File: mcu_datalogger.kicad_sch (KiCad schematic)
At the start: 25 parts, among them U1 DS1337S_, U3 24LC1025, U4 24LC1025, U5 ATMEGA328P-AU, Y1 32.768 KHz, Y2 16MHz

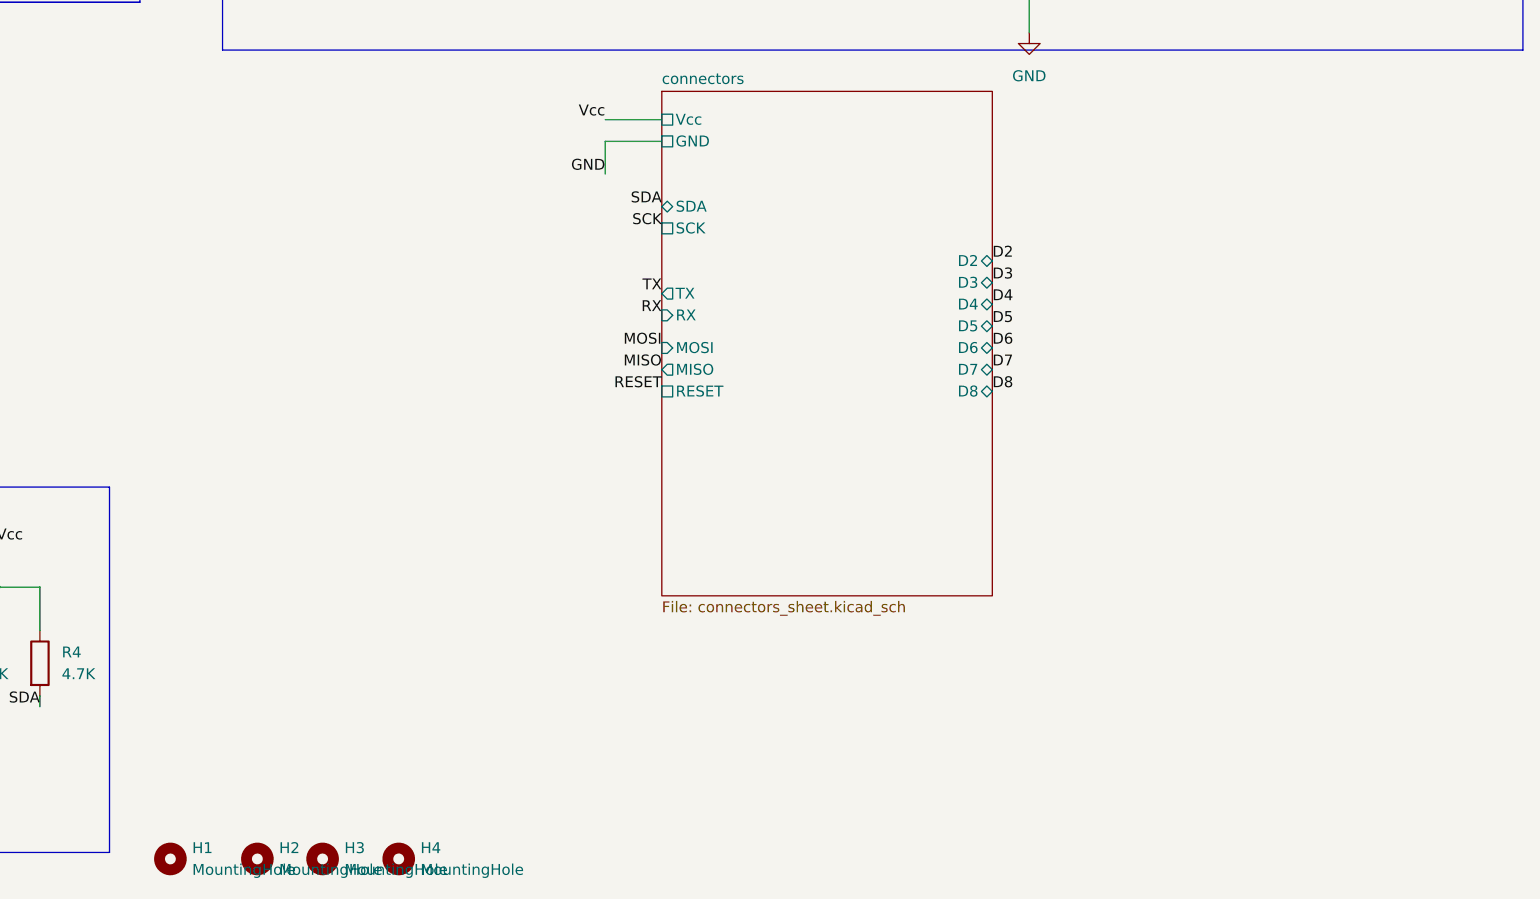
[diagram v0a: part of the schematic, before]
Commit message: Added all the Markings for Mounting Hole
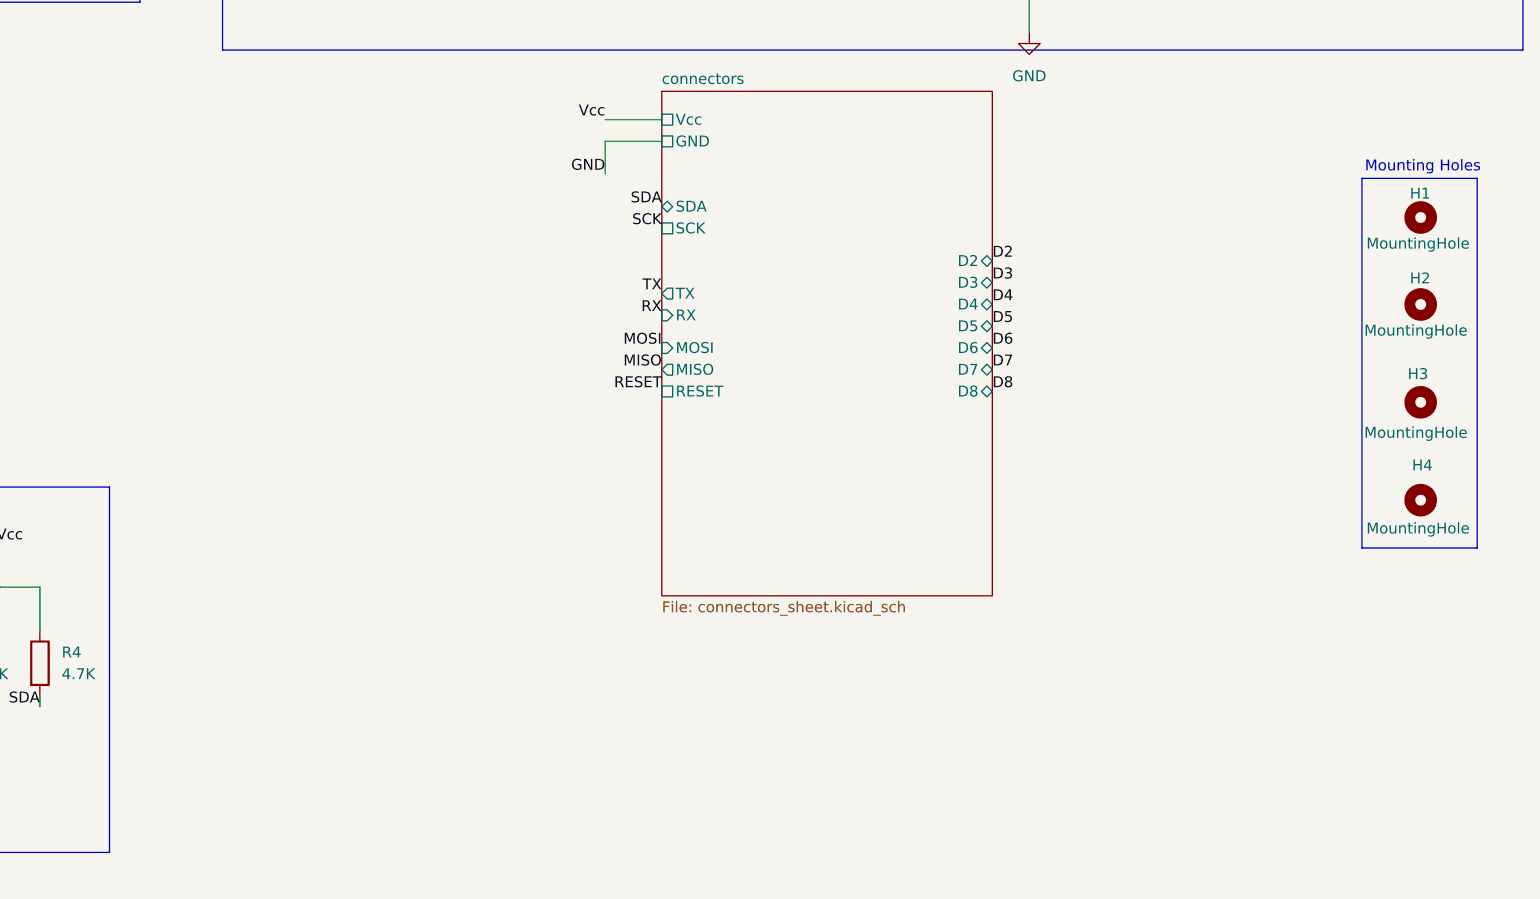
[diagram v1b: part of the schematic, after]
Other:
- note added: "Mounting Holes"
- moved on the sheet: H1, H2, H3, H4
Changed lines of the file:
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@@
+	)
+	(rectangle
+		(start 261.112 109.728)
+		(end 274.574 152.908)
+		(stroke
+			(width 0)
+			(type default)
+		)
+		(fill
+			(type none)
+		)
 	)
 	(rectangle
@@
 		(exclude_from_sim no)
 		(at 129.794 20.32 0)
+		(effects
+			(font
+				(size 1.27 1.27)
+			)
+		)
+	)
+	(text "Mounting Holes\n"
+		(exclude_from_sim no)
+		(at 268.224 108.458 0)
 		(effects
 			(font
@@
 	(symbol
 		(lib_id "Mechanical:MountingHole")
-		(at 132.08 189.23 0)
+		(at 267.97 124.46 0)
 		(unit 1)
 		(exclude_from_sim yes)
@@
 		(on_board yes)
 		(dnp no)
-		(fields_autoplaced yes)
 		(property "Reference" "H2"
-			(at 134.62 187.9599 0)
+			(at 266.7 121.412 0)
 			(effects
 				(font
@@
 		)
 		(property "Value" "MountingHole"
-			(at 134.62 190.4999 0)
+			(at 261.366 127.508 0)
 			(effects
 				(font
@@
 		)
 		(property "Footprint" "MountingHole:MountingHole_2.1mm"
-			(at 132.08 189.23 0)
+			(at 267.97 124.46 0)
 			(effects
 				(font
@@
 		)
 		(property "Datasheet" "~"
-			(at 132.08 189.23 0)
+			(at 267.97 124.46 0)
 			(effects
 				(font
@@
 		)
 		(property "Description" "Mounting Hole without connection"
-			(at 132.08 189.23 0)
+			(at 267.97 124.46 0)
 			(effects
 				(font
@@
 	(symbol
 		(lib_id "Mechanical:MountingHole")
-		(at 148.59 189.23 0)
+		(at 267.97 147.32 0)
 		(unit 1)
 		(exclude_from_sim yes)
@@
 		(on_board yes)
 		(dnp no)
-		(fields_autoplaced yes)
 		(property "Reference" "H4"
-			(at 151.13 187.9599 0)
+			(at 266.954 143.256 0)
 			(effects
 				(font
@@
 		)
 		(property "Value" "MountingHole"
-			(at 151.13 190.4999 0)
+			(at 261.62 150.622 0)
 			(effects
 				(font
@@
 		)
 		(property "Footprint" "MountingHole:MountingHole_2.1mm"
-			(at 148.59 189.23 0)
+			(at 267.97 147.32 0)
 			(effects
 				(font
@@
 		)
 		(property "Datasheet" "~"
-			(at 148.59 189.23 0)
+			(at 267.97 147.32 0)
 			(effects
 				(font
@@
 		)
 		(property "Description" "Mounting Hole without connection"
-			(at 148.59 189.23 0)
+			(at 267.97 147.32 0)
 			(effects
 				(font
@@
 	(symbol
 		(lib_id "Mechanical:MountingHole")
-		(at 139.7 189.23 0)
+		(at 267.97 135.89 0)
 		(unit 1)
 		(exclude_from_sim yes)
@@
 		(on_board yes)
 		(dnp no)
-		(fields_autoplaced yes)
 		(property "Reference" "H3"
-			(at 142.24 187.9599 0)
+			(at 266.446 132.588 0)
 			(effects
 				(font
@@
 		)
 		(property "Value" "MountingHole"
-			(at 142.24 190.4999 0)
+			(at 261.366 139.446 0)
 			(effects
 				(font
@@
 		)
 		(property "Footprint" "MountingHole:MountingHole_2.1mm"
-			(at 139.7 189.23 0)
+			(at 267.97 135.89 0)
 			(effects
 				(font
@@
 		)
 		(property "Datasheet" "~"
-			(at 139.7 189.23 0)
+			(at 267.97 135.89 0)
 			(effects
 				(font
@@
 		)
 		(property "Description" "Mounting Hole without connection"
-			(at 139.7 189.23 0)
+			(at 267.97 135.89 0)
 			(effects
 				(font
@@
 	(symbol
 		(lib_id "Mechanical:MountingHole")
-		(at 121.92 189.23 0)
+		(at 267.97 114.3 0)
 		(unit 1)
 		(exclude_from_sim yes)
@@
 		(on_board yes)
 		(dnp no)
-		(fields_autoplaced yes)
 		(property "Reference" "H1"
-			(at 124.46 187.9599 0)
+			(at 266.7 111.506 0)
 			(effects
 				(font
@@
 		)
 		(property "Value" "MountingHole"
-			(at 124.46 190.4999 0)
+			(at 261.62 117.348 0)
 			(effects
 				(font
@@
 		)
 		(property "Footprint" "MountingHole:MountingHole_2.1mm"
-			(at 121.92 189.23 0)
+			(at 267.97 114.3 0)
 			(effects
 				(font
@@
 		)
 		(property "Datasheet" "~"
-			(at 121.92 189.23 0)
+			(at 267.97 114.3 0)
 			(effects
 				(font
@@
 		)
 		(property "Description" "Mounting Hole without connection"
-			(at 121.92 189.23 0)
-			(effects
-				(font
+			(at 267.97 114.3 0)
+			(effects
+				(font

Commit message: Added PCB and Netlist(Power) as GND&VCC
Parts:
- U1: footprint DS1337S_:SOIC127P600X175-8N -> 530002B02500G:DS1337
- U5: footprint ATMEGA328P-AU:QFP80P900X900X120-32N -> Atmega_328P:QFP80P900X900X120-32N
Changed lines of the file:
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@@
-	(wire
-		(pts
-			(xy 172.72 109.22) (xy 172.72 105.41)
-		)
-		(stroke
-			(width 0)
-			(type default)
-		)
-	)
 	(wire
 		(pts
@@
 		(pts
 			(xy 222.25 85.09) (xy 222.25 92.71)
-		)
-		(stroke
-			(width 0)
-			(type default)
-		)
-	)
-	(wire
-		(pts
-			(xy 172.72 105.41) (xy 179.324 105.41)
 		)
 		(stroke
@@
 	(label "Vcc"
 		(at 66.04 170.18 180)
-		(fields_autoplaced yes)
 		(effects
 			(font
@@
 	(label "Vcc"
 		(at 176.53 80.01 180)
-		(fields_autoplaced yes)
 		(effects
 			(font
@@
 	(label "RX"
 		(at 219.71 41.91 0)
-		(fields_autoplaced yes)
 		(effects
 			(font
@@
 	(label "D5"
 		(at 218.44 54.61 0)
-		(fields_autoplaced yes)
 		(effects
 			(font
@@
 	(label "SCK"
 		(at 44.45 58.42 180)
-		(fields_autoplaced yes)
 		(effects
 			(font
@@
 	(label "SDA"
 		(at 57.15 165.1 0)
-		(fields_autoplaced yes)
 		(effects
 			(font
@@
 	(label "TX"
 		(at 219.71 44.45 0)
-		(fields_autoplaced yes)
 		(effects
 			(font
@@
 	(label "SDA"
 		(at 106.68 171.45 180)
-		(fields_autoplaced yes)
 		(effects
 			(font
@@
 	(label "Vcc"
 		(at 36.83 170.18 180)
-		(fields_autoplaced yes)
 		(effects
 			(font
@@
 	(label "D6"
 		(at 218.44 57.15 0)
-		(fields_autoplaced yes)
 		(effects
 			(font
@@
 	(label "SDA"
 		(at 44.45 66.04 180)
-		(fields_autoplaced yes)
 		(effects
 			(font
@@
 	(label "SCK"
 		(at 86.36 167.64 0)
-		(fields_autoplaced yes)
 		(effects
 			(font
@@
 	(label "Vcc"
 		(at 36.83 167.64 180)
-		(fields_autoplaced yes)
 		(effects
 			(font
@@
 	(label "RESET"
 		(at 187.96 80.01 180)
-		(fields_autoplaced yes)
 		(effects
 			(font
@@
 	(label "D2"
 		(at 218.44 46.99 0)
-		(fields_autoplaced yes)
 		(effects
 			(font
@@
 	(label "Vcc"
 		(at 76.2 160.02 0)
-		(fields_autoplaced yes)
 		(effects
 			(font
@@
 	(label "D3"
 		(at 218.44 49.53 0)
-		(fields_autoplaced yes)
 		(effects
 			(font
@@
 	(label "MOSI"
 		(at 187.96 49.53 180)
-		(fields_autoplaced yes)
 		(effects
 			(font
@@
 	(label "SCK"
 		(at 187.96 77.47 180)
-		(fields_autoplaced yes)
 		(effects
 			(font
@@
 	(label "SDA"
 		(at 187.96 74.93 180)
-		(fields_autoplaced yes)
 		(effects
 			(font
@@
 	(label "Vcc"
 		(at 101.6 152.4 0)
-		(fields_autoplaced yes)
 		(effects
 			(font
@@
 	(label "SCK"
 		(at 187.96 54.61 180)
-		(fields_autoplaced yes)
 		(effects
 			(font
@@
 	(label "MISO"
 		(at 187.96 52.07 180)
-		(fields_autoplaced yes)
 		(effects
 			(font
@@
 	(label "Vcc"
 		(at 36.83 165.1 180)
-		(fields_autoplaced yes)
 		(effects
 			(font
@@
 	(label "Vcc"
 		(at 46.99 160.02 180)
-		(fields_autoplaced yes)
 		(effects
 			(font
@@
 	(label "Vcc"
 		(at 66.04 165.1 180)
-		(fields_autoplaced yes)
 		(effects
 			(font
@@
 	(label "D7"
 		(at 218.44 59.69 0)
-		(fields_autoplaced yes)
 		(effects
 			(font
@@
 	)
 	(label "GND"
-		(at 172.72 109.22 180)
+		(at 179.07 105.41 180)
 		(effects
 			(font
@@
 	(label "D4"
 		(at 218.44 52.07 0)
-		(fields_autoplaced yes)
 		(effects
 			(font
@@
 	(label "SCK"
 		(at 57.15 167.64 0)
-		(fields_autoplaced yes)
 		(effects
 			(font
@@
 	(label "SCK"
 		(at 96.52 171.45 180)
-		(fields_autoplaced yes)
 		(effects
 			(font
@@
 	(label "SDA"
 		(at 86.36 165.1 0)
-		(fields_autoplaced yes)
 		(effects
 			(font
@@
 	(label "D8"
 		(at 187.96 41.91 180)
-		(fields_autoplaced yes)
 		(effects
 			(font
@@
 			)
 		)
-		(property "Footprint" "ATMEGA328P-AU:QFP80P900X900X120-32N"
+		(property "Footprint" "Atmega_328P:QFP80P900X900X120-32N"
 			(at 203.2 59.69 0)
 			(effects
@@
 			)
 		)
-		(property "Footprint" "DS1337S_:SOIC127P600X175-8N"
+		(property "Footprint" "530002B02500G:DS1337"
 			(at 62.23 66.04 0)
 			(effects

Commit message: PCB Layout Started
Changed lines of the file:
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@@
-	(wire
-		(pts
-			(xy 172.72 102.87) (xy 179.324 102.87)
-		)
-		(stroke
-			(width 0)
-			(type default)
-		)
-	)
 	(wire
 		(pts
@@
 		)
 	)
+	(label "GND"
+		(at 179.324 105.41 180)
+		(effects
+			(font
+				(size 1.27 1.27)
+			)
+			(justify right bottom)
+		)
+	)
 	(label "RESET"
 		(at 179.324 134.62 180)
@@
 		)
 	)
+	(label "Vcc"
+		(at 179.324 102.87 180)
+		(effects
+			(font
+				(size 1.27 1.27)
+			)
+			(justify right bottom)
+		)
+	)
 	(label "SCK"
 		(at 187.96 54.61 180)
@@
 		)
 	)
-	(label "GND"
-		(at 179.07 105.41 180)
-		(effects
-			(font
-				(size 1.27 1.27)
-			)
-			(justify right bottom)
-		)
-	)
-	(label "Vcc"
-		(at 172.72 102.87 180)
-		(effects
-			(font
-				(size 1.27 1.27)
-			)
-			(justify right bottom)
-		)
-	)

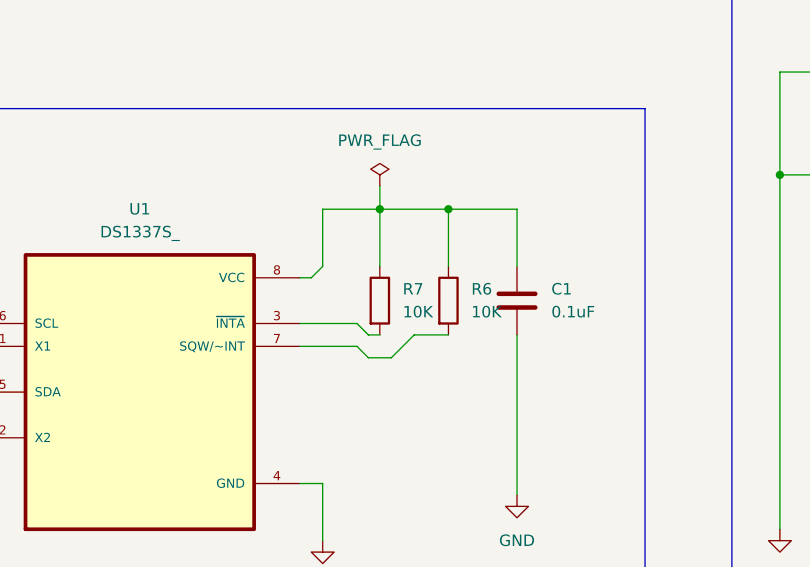
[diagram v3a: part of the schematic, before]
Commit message: Added the Zones for GND & VCC
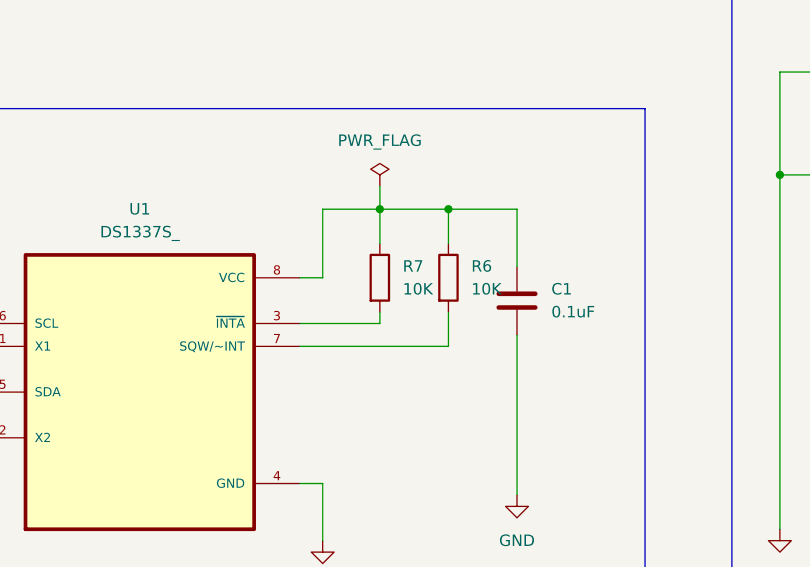
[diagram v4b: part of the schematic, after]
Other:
- moved on the sheet: R6, R7
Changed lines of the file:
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@@
 	(wire
 		(pts
-			(xy 82.55 76.2) (xy 82.55 82.55)
+			(xy 80.01 58.42) (xy 88.9 58.42)
 		)
 		(stroke
@@
 	(wire
 		(pts
-			(xy 80.01 76.2) (xy 82.55 76.2)
+			(xy 82.55 76.2) (xy 82.55 82.55)
 		)
 		(stroke
@@
 	(wire
 		(pts
-			(xy 80.01 60.96) (xy 86.36 60.96)
+			(xy 80.01 76.2) (xy 82.55 76.2)
 		)
 		(stroke
@@
 	(wire
 		(pts
-			(xy 80.01 58.42) (xy 86.36 58.42)
+			(xy 88.9 45.72) (xy 88.9 49.53)
 		)
 		(stroke
@@
 	(wire
 		(pts
-			(xy 88.9 45.72) (xy 88.9 52.07)
+			(xy 104.14 45.72) (xy 104.14 52.07)
 		)
 		(stroke
@@
 	(wire
 		(pts
-			(xy 104.14 45.72) (xy 104.14 52.07)
+			(xy 82.55 53.34) (xy 80.01 53.34)
 		)
 		(stroke
@@
 	(wire
 		(pts
-			(xy 82.55 52.07) (xy 81.28 53.34)
-		)
-		(stroke
-			(width 0)
-			(type default)
-		)
-	)
-	(wire
-		(pts
 			(xy 218.44 82.55) (xy 220.98 82.55)
 		)
@@
 	(wire
 		(pts
-			(xy 96.52 45.72) (xy 96.52 52.07)
+			(xy 96.52 45.72) (xy 96.52 49.53)
 		)
 		(stroke
@@
 	(wire
 		(pts
-			(xy 87.63 62.23) (xy 90.17 62.23)
-		)
-		(stroke
-			(width 0)
-			(type default)
-		)
-	)
-	(wire
-		(pts
 			(xy 76.2 175.26) (xy 76.2 180.34)
 		)
@@
 	(wire
 		(pts
+			(xy 88.9 58.42) (xy 88.9 57.15)
+		)
+		(stroke
+			(width 0)
+			(type default)
+		)
+	)
+	(wire
+		(pts
 			(xy 60.96 175.26) (xy 76.2 175.26)
 		)
@@
 	(wire
 		(pts
-			(xy 81.28 53.34) (xy 80.01 53.34)
-		)
-		(stroke
-			(width 0)
-			(type default)
-		)
-	)
-	(wire
-		(pts
 			(xy 157.48 63.5) (xy 167.64 63.5)
 		)
@@
 	(wire
 		(pts
-			(xy 92.71 59.69) (xy 96.52 59.69)
-		)
-		(stroke
-			(width 0)
-			(type default)
-		)
-	)
-	(wire
-		(pts
 			(xy 180.34 30.48) (xy 180.34 39.37)
 		)
@@
 	(wire
 		(pts
-			(xy 87.63 59.69) (xy 88.9 59.69)
-		)
-		(stroke
-			(width 0)
-			(type default)
-		)
-	)
-	(wire
-		(pts
 			(xy 31.75 71.12) (xy 44.45 71.12)
 		)
@@
 	(wire
 		(pts
-			(xy 90.17 62.23) (xy 92.71 59.69)
-		)
-		(stroke
-			(width 0)
-			(type default)
-		)
-	)
-	(wire
-		(pts
-			(xy 82.55 45.72) (xy 82.55 52.07)
+			(xy 82.55 45.72) (xy 82.55 53.34)
 		)
 		(stroke
@@
 	(wire
 		(pts
-			(xy 265.43 34.29) (xy 265.43 36.83)
+			(xy 80.01 60.96) (xy 96.52 60.96)
 		)
 		(stroke
@@
 	(wire
 		(pts
-			(xy 220.98 85.09) (xy 222.25 85.09)
+			(xy 265.43 34.29) (xy 265.43 36.83)
 		)
 		(stroke
@@
 	(wire
 		(pts
-			(xy 88.9 43.18) (xy 88.9 45.72)
+			(xy 220.98 85.09) (xy 222.25 85.09)
 		)
 		(stroke
@@
 	(wire
 		(pts
-			(xy 96.52 157.48) (xy 101.6 157.48)
+			(xy 88.9 43.18) (xy 88.9 45.72)
 		)
 		(stroke
@@
 	(wire
 		(pts
-			(xy 180.34 54.61) (xy 187.96 54.61)
+			(xy 96.52 157.48) (xy 101.6 157.48)
 		)
 		(stroke
@@
 	(wire
 		(pts
-			(xy 86.36 58.42) (xy 87.63 59.69)
+			(xy 180.34 54.61) (xy 187.96 54.61)
 		)
 		(stroke
@@
 	(wire
 		(pts
-			(xy 139.7 55.88) (xy 149.86 55.88)
+			(xy 96.52 57.15) (xy 96.52 60.96)
 		)
 		(stroke
@@
 	(wire
 		(pts
-			(xy 184.15 80.01) (xy 187.96 80.01)
+			(xy 139.7 55.88) (xy 149.86 55.88)
 		)
 		(stroke
@@
 	(wire
 		(pts
-			(xy 180.34 39.37) (xy 187.96 39.37)
+			(xy 184.15 80.01) (xy 187.96 80.01)
 		)
 		(stroke
@@
 	(wire
 		(pts
-			(xy 86.36 60.96) (xy 87.63 62.23)
+			(xy 180.34 39.37) (xy 187.96 39.37)
 		)
 		(stroke
@@
 	(symbol
 		(lib_id "Device:R")
-		(at 96.52 55.88 0)
+		(at 96.52 53.34 0)
 		(unit 1)
 		(exclude_from_sim no)
@@
 		(fields_autoplaced yes)
 		(property "Reference" "R6"
-			(at 99.06 54.6099 0)
+			(at 99.06 52.0699 0)
 			(effects
 				(font
@@
 		)
 		(property "Value" "10K"
-			(at 99.06 57.1499 0)
+			(at 99.06 54.6099 0)
 			(effects
 				(font
@@
 		)
 		(property "Footprint" "Resistor_SMD:R_0805_2012Metric"
-			(at 94.742 55.88 90)
+			(at 94.742 53.34 90)
 			(effects
 				(font
@@
 		)
 		(property "Datasheet" "~"
-			(at 96.52 55.88 0)
+			(at 96.52 53.34 0)
 			(effects
 				(font
@@
 		)
 		(property "Description" "Resistor"
-			(at 96.52 55.88 0)
+			(at 96.52 53.34 0)
 			(effects
 				(font
@@
 	(symbol
 		(lib_id "Device:R")
-		(at 88.9 55.88 0)
+		(at 88.9 53.34 0)
 		(unit 1)
 		(exclude_from_sim no)
@@
 		(fields_autoplaced yes)
 		(property "Reference" "R7"
-			(at 91.44 54.6099 0)
+			(at 91.44 52.0699 0)
 			(effects
 				(font
@@
 		)
 		(property "Value" "10K"
-			(at 91.44 57.1499 0)
+			(at 91.44 54.6099 0)
 			(effects
 				(font
@@
 		)
 		(property "Footprint" "Resistor_SMD:R_0805_2012Metric"
-			(at 87.122 55.88 90)
+			(at 87.122 53.34 90)
 			(effects
 				(font
@@
 		)
 		(property "Datasheet" "~"
-			(at 88.9 55.88 0)
+			(at 88.9 53.34 0)
 			(effects
 				(font
@@
 		)
 		(property "Description" "Resistor"
-			(at 88.9 55.88 0)
+			(at 88.9 53.34 0)
 			(effects
 				(font
